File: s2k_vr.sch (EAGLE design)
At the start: 58 parts, among them IC1 MKE04Z8VWJ4, IC2 MAX9926, IC3 LTC6903, IC4 74LVC2G32DP, Q1 12MHz

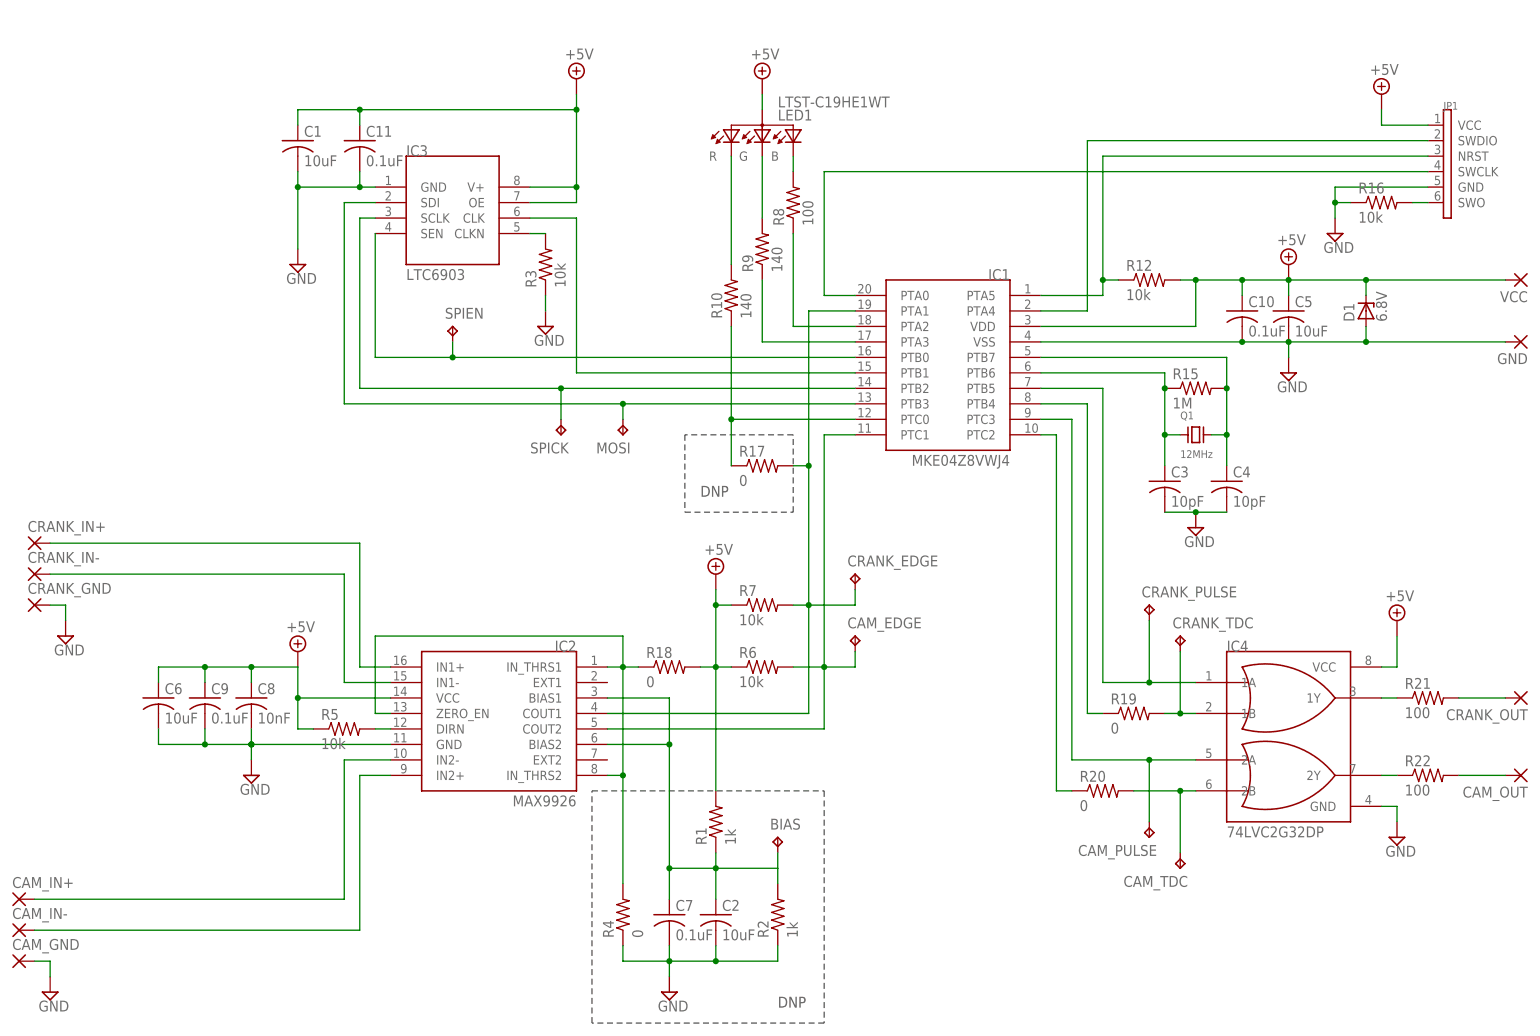
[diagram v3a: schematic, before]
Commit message: Completed board layout
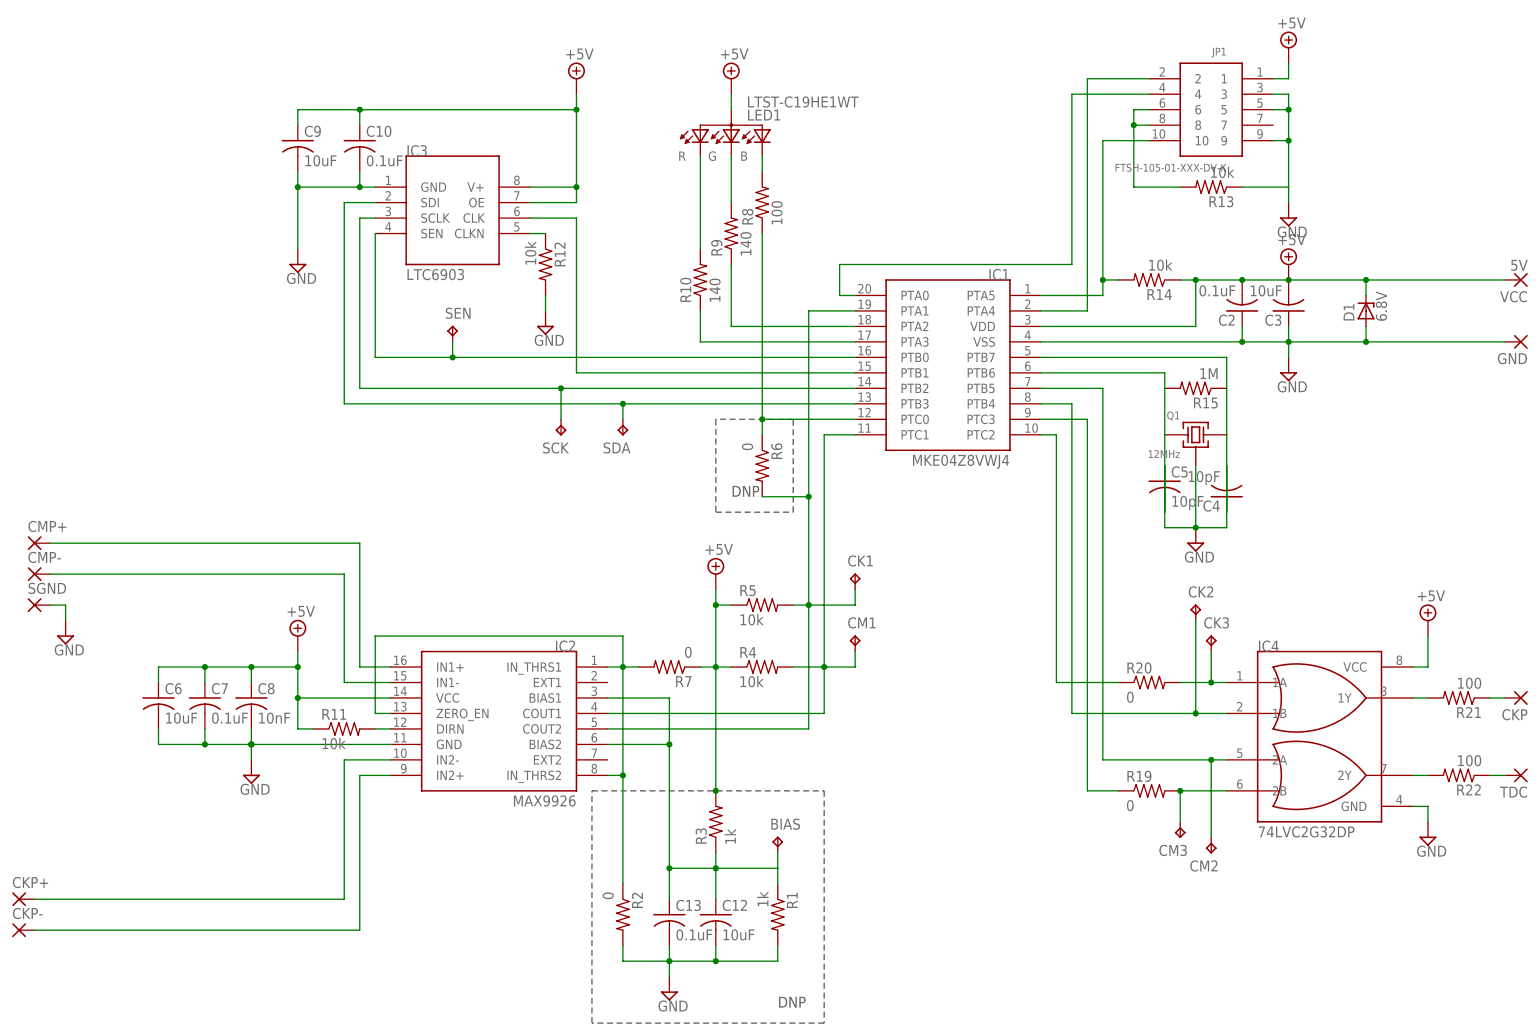
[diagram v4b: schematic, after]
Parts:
- removed C1: 10uF, resistor:C-USC0805
- removed C11: 0.1uF, resistor:C-USC0603
- removed CAM_GND, CAM_IN+, CAM_IN-, CAM_OUT, CRANK_GND, CRANK_IN+, CRANK_IN-, CRANK_OUT: (no value), wirepad:3,17/1,1
- removed CAM_PULSE, CAM_TDC, CRANK_PULSE, CRANK_TDC: TPB2,54, testpad:TPB2,54
- removed R16: 10k, resistor:R-US_R0603
- removed R17, R18: 0, resistor:R-US_R0603
- added C12: 10uF, resistor:C-USC0603
- added C13: 0.1uF, resistor:C-USC0603
- added CK2, CK3, CM2, CM3: TPB2,54, testpad:TPB2,54
- added CKP, CKP+, CKP-, CMP+, CMP-, SGND, TDC: (no value), wirepad:3,81/1,4
- added R11, R13, R14: 10k, resistor:R-US_R0603
- C2: value 10uF -> 0.1uF
- C3: value 10pF -> 10uF; device resistor:C-USC0603 -> resistor:C-USC0805
- C5: value 10uF -> 10pF; device resistor:C-USC0805 -> resistor:C-USC0603
- C9: value 0.1uF -> 10uF; device resistor:C-USC0603 -> resistor:C-USC0805
- GND: device wirepad:3,17/1,1 -> wirepad:3,81/1,4
- JP1: value TC2030 -> FTSH-105-01-XXX-DV-K; device parts:TC2030 -> FTSH-105-XX-XX-DV-K:FTSH-105-01-XXX-DV-K
- R2: value 1k -> 0
- R3: value 10k -> 1k
- R4: value 0 -> 10k
- R6, R7: value 10k -> 0
- VCC: value (none) -> 5V; device wirepad:3,17/1,1 -> wirepad:3,81/1,4
- renumbered CAM_EDGE to CM1, CRANK_EDGE to CK1, MOSI to SDA, SPICK to SCK, SPIEN to SEN
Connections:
- net N$14 renamed SPIEN
- net N$3 renamed SPICK
- net N$4 renamed MOSI
- net N$7 renamed CLK
- removed net N$1: CK1.TP, IC1.PTA1, IC2.COUT1, R17.2, R7.2
- removed net N$11: IC1.PTA5, JP1.NRST, R12.1
- removed net N$16: CRANK_PULSE.TP, IC1.PTB5, IC4.1A
- removed net N$18: CAM_PULSE.TP, IC1.PTC3, IC4.2A
- removed net N$2: CAM_IN-.P, IC2.IN2+
- removed net N$23: CRANK_OUT.P, R21.2
- removed net N$27: CAM_IN+.P, IC2.IN2-
- removed net N$28: IC1.PTC0, R10.1, R17.1
- removed net N$30: C4.1, IC1.PTB7, Q1.2, R15.2
- removed net N$31: CM1.TP, IC1.PTC1, IC2.COUT2, R6.2
- removed net N$34: CRANK_IN-.P, IC2.IN1-
- removed net N$37: CRANK_TDC.TP, IC4.1B, R19.2
- removed net N$38: CAM_TDC.TP, IC4.2B, R20.2
- removed net N$40: CAM_OUT.P, R22.2
- removed net N$8: IC1.PTA0, JP1.SWCLK
- new net CAM_EDGE: CM1.TP, IC1.PTC1, IC2.COUT1, R4.2
- new net CAM_IN+: CKP+.P, IC2.IN2-
- new net CAM_IN-: CKP-.P, IC2.IN2+
- new net CAM_OUT: R22.1, TDC.P
- new net CAM_PULSE: CK2.TP, IC1.PTB4, IC4.1B
- new net CAM_TDC: CK3.TP, IC4.1A, R20.2
- new net CRANK_EDGE: CK1.TP, IC1.PTA1, IC2.COUT2, R5.2, R6.2
- new net CRANK_IN+: CMP+.P, IC2.IN1+
- new net CRANK_IN-: CMP-.P, IC2.IN1-
- new net CRANK_OUT: CKP.P, R21.1
- new net CRANK_PULSE: CM2.TP, IC1.PTB5, IC4.2A
- new net N$14: IC1.PTC0, R6.1, R8.1
- new net NRST: IC1.PTA5, JP1.10, R14.2
- new net SWCLK: IC1.PTA0, JP1.4
- new net SWDIO: IC1.PTA4, JP1.2
- net +5V: now also C2.2, C3.2, C7.1, JP1.1, R11.1, R14.1, R3.2, R4.1; no longer C1.1, C11.1, C5.1, JP1.VCC, R1.2, R12.2, R18.2, R6.1
- net GND: now also C12.2, C13.2, C2.1, C3.1, C5.1, JP1.3, JP1.5, JP1.9, Q1.GND, R1.2, R12.2, R13.1, R2.2, SGND.P; no longer C1.2, C11.2, C2.2, C3.2, C5.2, CAM_GND.P, CRANK_GND.P, JP1.GND, R16.1, R2.1, R3.1, R4.1
- net N$10: now also C4.1, IC1.PTB7, Q1.1, R15.1; no longer IC1.PTA4, JP1.SWDIO
- net N$12: now also R10.1; no longer R9.1
- net N$13: now also R12.1; no longer R3.2
- net N$15: now also IC1.PTC3; no longer IC1.PTB4
- net N$19: now also C12.1, C13.1, R3.1; no longer C2.1, C7.1, R2.2
- net N$21: now also R21.2; no longer R21.1
- net N$24: now also JP1.6, JP1.8, R13.2; no longer CRANK_IN+.P, IC2.IN1+
- net N$25: now also CM3.TP, IC4.2B, R19.2; no longer JP1.SWO, R16.2
- net N$26: now also C5.2, Q1.2, R15.2; no longer C3.1, Q1.1, R15.1
- net N$36: now also R2.1, R7.2; no longer R18.1, R4.2
- net N$39: now also R22.2; no longer R22.1
- net N$5: now also R11.2; no longer R5.2
- net N$6: now also R9.1; no longer R8.1
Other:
- moved on the sheet: C10, C2, C3, C4, C5, C7, C9, IC4, LED1, R1, R10, R12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
